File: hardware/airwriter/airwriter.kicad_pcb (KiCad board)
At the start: 2 copper layers, 62 x 104.3 mm, 130 parts, among them J1 USB-C 5V in, J2 Mini-DIN-8 to printer, J4 Mini-DIN-8 LocalTalk, SW1 EVQP44B3M side-press, SW3 TS-1002-BR16026, U1 ESP32-S3-WROOM-1-N8R2, U2 MAX3490ESA+, U3 MAX3232ESE+, U4 AP7361C-33E, U5 USBLC6-2SC6, U6 SP3485EN-L, U7 PIC12F1840-I/P, U8 SP3485EN-L, U9 74AHCT1G125SE-7

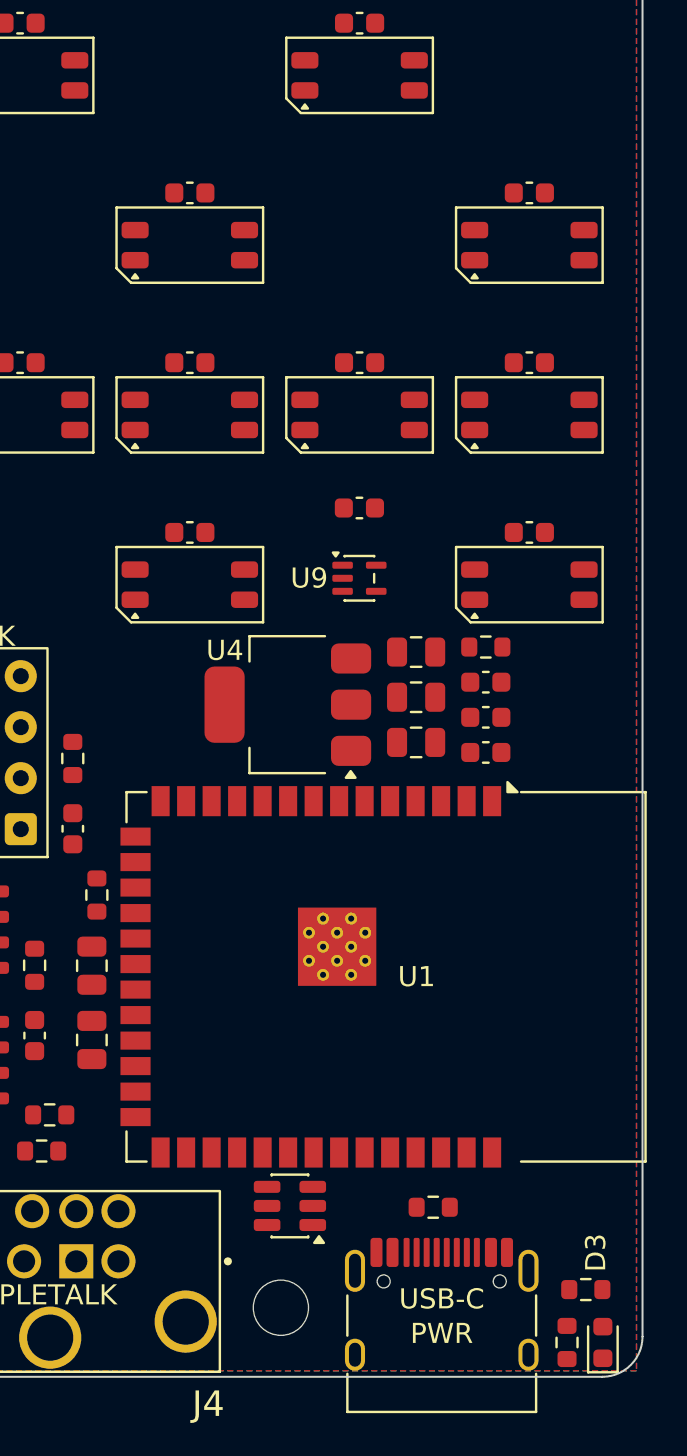
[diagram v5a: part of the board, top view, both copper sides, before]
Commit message: Lift the module for the corner mount
The two lower mounts sit level now, on the same columns as the upper pair:
H3 (105.636, 151.930) and H4 (156.364, 151.930). Four holes, one
rectangle, 50.7 x 86.3mm, support hull 505 -> 4378mm2.

H4's y is read off H3 rather than typed, so "level" is a property of the
placement instead of two numbers someone has to remember to edit together.
That makes J2 -- which caps H3 at y <= 152.034 -- set both, and it takes
J1 out of the picture: J1 alone would have allowed 154.214, and the level
pair sits north of that.

U1 lifts 4.556mm north to (149.250, 139.794), the minimum that clears
H4's courtyard by 0.2mm. Its south pad row gains 4.6mm to J4, so round
6's /HSKI_DRV pinch is far better than it was.

THE ANTENNA PAYS FOR THIS, on both edges, and the numbers are the point:

  north   the keepout's edge is clamped at the grid boundary y=127.6 so it
          stays out of the LED field, giving up 2.556mm of the lift. RF
          margin north of the radiator: 5.750 -> 3.194mm.
  south   notched around H4: on a 3.009mm-wide strip the clearance goes
          5.750 -> 0.495mm. Radiator south edge y=148.794; H4's drill edge
          is 1.761mm south of it, its courtyard 0.695mm, and a 5mm nut or
          boss would come within 0.636mm.

The lift closes the north-east strip to a band 2.094mm tall once a 1.0mm
escape channel is reserved above U1's north pad row -- reserved before
placing, not recovered after, because fourteen signals leave that row and
a distance-minimising solver packs caps straight onto it. That is how
round 6 lost /HSKI_DRV on the other side.

The band seats three parts, not five: dot (7,4)'s lit envelope blocks its
west end and (7,6)'s its east. So C9 (U1's rail 100n) takes 3.29mm from
pad 2, C2 (the 10u bulk) 6.32mm and C6 (the EN cap) 8.01mm, ordered by
what the module needs nearest rather than by package size. C5 is a
supplementary 100n redundant with C9 and R3 is a pull-up free on its own
nets, so those two travel 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
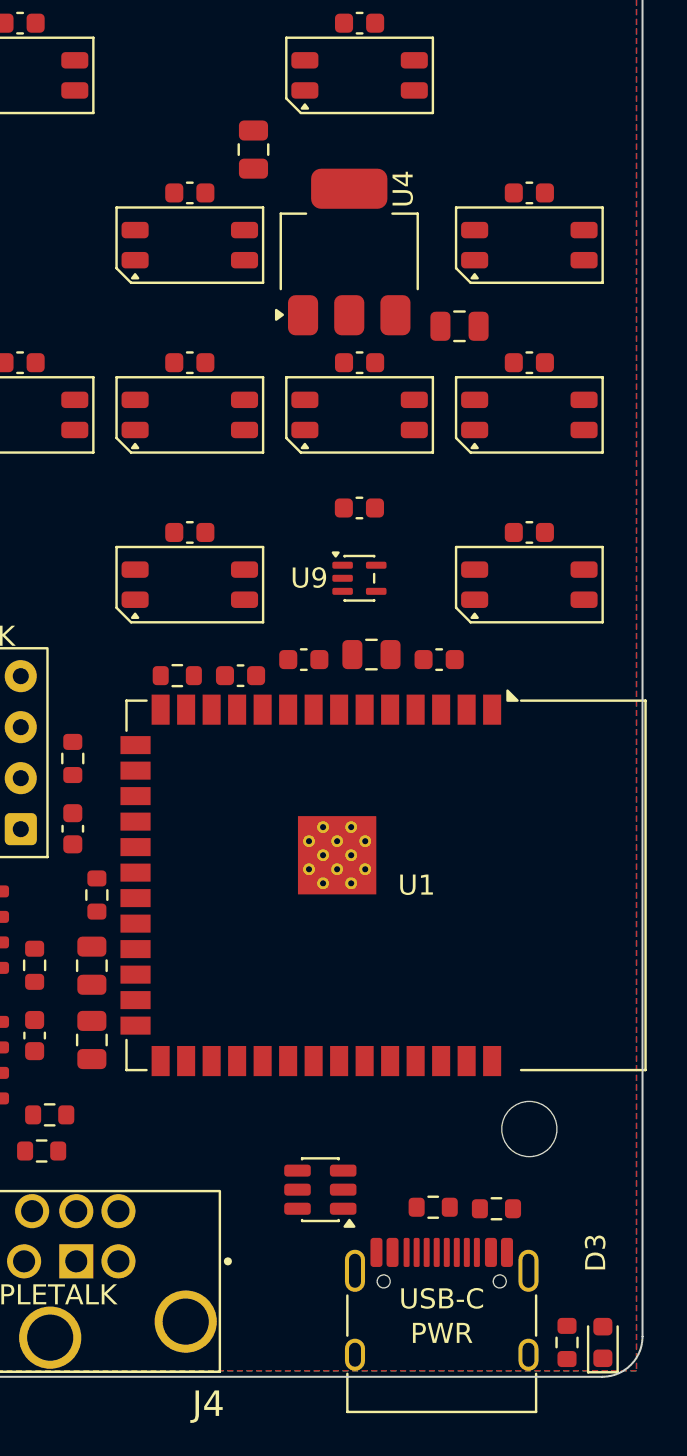
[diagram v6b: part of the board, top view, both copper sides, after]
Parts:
- moved C21 30.6 mm to (142.6, 103.2), turned to 90 degrees
- moved U4 22.8 mm to (147.4, 108.2), turned to 90 degrees
- moved C4 16.4 mm to (152.9, 112.0)
- moved R3 15.4 mm to (138.8, 129.3)
- moved H4 15.2 mm to (156.4, 151.9)
- moved C5 12.2 mm to (142.0, 129.3)
- moved C6 9.51 mm to (145.1, 128.6)
- moved R2 6.00 mm to (154.7, 155.9)
- moved C9 5.18 mm to (151.9, 128.6)
- moved U1 4.56 mm to (149.2, 139.8)
- moved C2 3.08 mm to (148.5, 128.3)
- moved U5 1.72 mm to (146.0, 154.9)
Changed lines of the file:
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@@
 	(footprint "Capacitor_SMD:C_0805_2012Metric"
 		(layer "F.Cu")
-		(at 150.725 130.425)
+		(at 148.5 128.3)
 		(descr "Capacitor SMD 0805 (2012 Metric), square (rectangular) end terminal, IPC-7351 nominal, (Body size source: IPC-SM-782 page 76, https://www.pcb-3d.com/wordpress/wp-content/uploads/ipc-sm-782a_amendment_1_and_2.pdf, https://docs.google.com/spreadsheets/d/1BsfQQcO9C6DZCsRaXUlFlo91Tg2WpOkGARC1WS5S8t0/edit?usp=sharing)")
 		(tags "capacitor")
@@
 	(footprint "Capacitor_SMD:C_0805_2012Metric"
 		(layer "F.Cu")
-		(at 150.725 128.175)
+		(at 152.884 111.95)
 		(descr "Capacitor SMD 0805 (2012 Metric), square (rectangular) end terminal, IPC-7351 nominal, (Body size source: IPC-SM-782 page 76, https://www.pcb-3d.com/wordpress/wp-content/uploads/ipc-sm-782a_amendment_1_and_2.pdf, https://docs.google.com/spreadsheets/d/1BsfQQcO9C6DZCsRaXUlFlo91Tg2WpOkGARC1WS5S8t0/edit?usp=sharing)")
 		(tags "capacitor")
@@
 	(footprint "Capacitor_SMD:C_0603_1608Metric"
 		(layer "F.Cu")
-		(at 154.195 133.175)
+		(at 151.87 128.55)
 		(descr "Capacitor SMD 0603 (1608 Metric), square (rectangular) end terminal, IPC-7351 nominal, (Body size source: IPC-SM-782 page 76, https://www.pcb-3d.com/wordpress/wp-content/uploads/ipc-sm-782a_amendment_1_and_2.pdf)")
 		(tags "capacitor")
@@
 	(footprint "Resistor_SMD:R_0603_1608Metric"
 		(layer "F.Cu")
-		(at 154.195 127.925)
+		(at 138.83 129.35)
 		(descr "Resistor SMD 0603 (1608 Metric), square (rectangular) end terminal, IPC-7351 nominal, (Body size source: IPC-SM-782 page 72, https://www.pcb-3d.com/wordpress/wp-content/uploads/ipc-sm-782a_amendment_1_and_2.pdf)")
 		(tags "resistor")
@@
 	(footprint "Package_TO_SOT_SMD:SOT-223-3_TabPin2"
 		(layer "F.Cu")
-		(at 144.335 130.795 180)
+		(at 147.394 108.25 90)
 		(descr "module CMS SOT223 4 pins")
 		(tags "CMS SOT")
 		(property "Reference" "U4"
-			(at 3.135 2.695 180)
+			(at 3.135 2.695 90)
 			(layer "F.SilkS")
 			(effects
@@
 		)
 		(property "Value" "AP7361C-33E"
-			(at 0 4.5 180)
+			(at 0 4.5 90)
 			(layer "F.Fab")
 			(effects
@@
 		)
 		(property "Datasheet" ""
-			(at 0 0 180)
+			(at 0 0 90)
 			(unlocked yes)
 			(layer "F.Fab")
@@
 		)
 		(property "Description" "LDO regulator, 3.3V fixed, 1A, SOT-223"
-			(at 0 0 180)
+			(at 0 0 90)
 			(unlocked yes)
 			(layer "F.Fab")
@@
 		)
 		(property "MPN" "AP7361C-33E-13"
-			(at 0 0 180)
+			(at 0 0 90)
 			(unlocked yes)
 			(layer "F.Fab")
@@
 		)
 		(property "Manufacturer" "Diodes Incorporated"
-			(at 0 0 180)
+			(at 0 0 90)
 			(unlocked yes)
 			(layer "F.Fab")
@@
 		(duplicate_pad_numbers_are_jumpers no)
 		(fp_line
-			(start 1.91 3.41)
-			(end 1.91 2.15)
+			(start 1.91 -3.41)
+			(end 1.91 -2.15)
 			(stroke
 				(width 0.12)
@@
 		)
 		(fp_line
-			(start 1.91 -3.41)
-			(end 1.91 -2.15)
+			(start -1.85 -3.41)
+			(end 1.91 -3.41)
 			(stroke
 				(width 0.12)
@@
 		)
 		(fp_line
-			(start -1.85 3.41)
-			(end 1.91 3.41)
+			(start 1.91 3.41)
+			(end 1.91 2.15)
 			(stroke
 				(width 0.12)
@@
 		)
 		(fp_line
-			(start -1.85 -3.41)
-			(end 1.91 -3.41)
+			(start -1.85 3.41)
+			(end 1.91 3.41)
 			(stroke
 				(width 0.12)
@@
 		)
 		(fp_line
-			(start 4.4 3.6)
-			(end 4.4 -3.6)
+			(start 4.4 -3.6)
+			(end -4.4 -3.6)
 			(stroke
 				(width 0.05)
@@
 		)
 		(fp_line
-			(start 4.4 -3.6)
-			(end -4.4 -3.6)
+			(start -4.4 -3.6)
+			(end -4.4 3.6)
 			(stroke
 				(width 0.05)
@@
 		)
 		(fp_line
-			(start -4.4 3.6)
-			(end 4.4 3.6)
+			(start 4.4 3.6)
+			(end 4.4 -3.6)
 			(stroke
 				(width 0.05)
@@
 		)
 		(fp_line
-			(start -4.4 -3.6)
-			(end -4.4 3.6)
+			(start -4.4 3.6)
+			(end 4.4 3.6)
 			(stroke
 				(width 0.05)
@@
 		)
 		(fp_line
-			(start -1.85 3.35)
-			(end 1.85 3.35)
+			(start -1.85 -2.35)
+			(end -0.85 -3.35)
 			(stroke
 				(width 0.1)
@@
 		(fp_line
 			(start -1.85 -2.35)
-			(end -0.85 -3.35)
+			(end -1.85 3.35)
 			(stroke
 				(width 0.1)
@@
 		)
 		(fp_line
-			(start -1.85 -2.35)
-			(end -1.85 3.35)
+			(start -1.85 3.35)
+			(end 1.85 3.35)
 			(stroke
 				(width 0.1)
@@
 		)
 		(fp_text user "${REFERENCE}"
-			(at 0 0 270)
+			(at 0 0 180)
 			(layer "F.Fab")
 			(effects
@@
 		)
 		(pad "1" smd roundrect
-			(at -3.15 -2.3 180)
+			(at -3.15 -2.3 90)
 			(size 2 1.5)
 			(layers "F.Cu" "F.Mask" "F.Paste")
@@
 		)
 		(pad "2" smd roundrect
-			(at -3.15 0 180)
+			(at -3.15 0 90)
 			(size 2 1.5)
 			(layers "F.Cu" "F.Mask" "F.Paste")
@@
 		)
 		(pad "2" smd roundrect
-			(at 3.15 0 180)
+			(at 3.15 0 90)
 			(size 2 3.8)
 			(layers "F.Cu" "F.Mask" "F.Paste")
@@
 		)
 		(pad "3" smd roundrect
-			(at -3.15 2.3 180)
+			(at -3.15 2.3 90)
 			(size 2 1.5)
 			(layers "F.Cu" "F.Mask" "F.Paste")
@@
 	(footprint "Capacitor_SMD:C_0805_2012Metric"
 		(layer "F.Cu")
-		(at 150.725 132.675)
+		(at 142.624 103.15 90)
 		(descr "Capacitor SMD 0805 (2012 Metric), square (rectangular) end terminal, IPC-7351 nominal, (Body size source: IPC-SM-782 page 76, https://www.pcb-3d.com/wordpress/wp-content/uploads/ipc-sm-782a_amendment_1_and_2.pdf, https://docs.google.com/spreadsheets/d/1BsfQQcO9C6DZCsRaXUlFlo91Tg2WpOkGARC1WS5S8t0/edit?usp=sharing)")
 		(tags "capacitor")
 		(property "Reference" "C21"
-			(at 0 -1.68 0)
+			(at 0 -1.68 90)
 			(layer "F.Fab")
 			(effects
@@
 		)
 		(property "Value" "22u"
-			(at 0 1.68 0)
+			(at 0 1.68 90)
 			(layer "F.Fab")
 			(effects
@@
 		)
 		(property "Datasheet" ""
-			(at 0 0 0)
+			(at 0 0 90)
 			(layer "F.Fab")
 			(hide yes)
@@
 		)
 		(property "Description" ""
-			(at 0 0 0)
+			(at 0 0 90)
 			(layer "F.Fab")
 			(hide yes)
@@
 		)
 		(property "KiLib_Generator" "SMD_2terminal_chip_molded"
-			(at 0 0 0)
+			(at 0 0 90)
 			(layer "F.SilkS")
 			(hide yes)
@@
 		)
 		(fp_text user "${REFERENCE}"
-			(at 0 0 0)
+			(at 0 0 90)
 			(layer "F.Fab")
 			(effects
@@
 		)
 		(pad "1" smd roundrect
-			(at -0.95 0)
+			(at -0.95 0 90)
 			(size 1 1.45)
 			(layers "F.Cu" "F.Mask" "F.Paste")
@@
 		)
 		(pad "2" smd roundrect
-			(at 0.95 0)
+			(at 0.95 0 90)
 			(size 1 1.45)
 			(layers "F.Cu" "F.Mask" "F.Paste")
@@
 	(footprint "Resistor_SMD:R_0603_1608Metric"
 		(layer "F.Cu")
-		(at 159.175 159.925)
+		(at 154.725 155.9)
 		(descr "Resistor SMD 0603 (1608 Metric), square (rectangular) end terminal, IPC-7351 nominal, (Body size source: IPC-SM-782 page 72, https://www.pcb-3d.com/wordpress/wp-content/uploads/ipc-sm-782a_amendment_1_and_2.pdf)")
 		(tags "resistor")
@@
 	(footprint "RF_Module:ESP32-S3-WROOM-1"
 		(layer "F.Cu")
-		(at 149.25 144.35 -90)
+		(at 149.25 139.794 -90)
 		(descr "2.4 GHz Wi-Fi and Bluetooth module  https://www.espressif.com/sites/default/files/documentation/esp32-s3-wroom-1_wroom-1u_datasheet_en.pdf")
 		(tags "2.4 GHz Wi-Fi and Bluetooth module")
@@
 			(polygon
 				(pts
-					(xy 156 129.6) (xy 162 129.6) (xy 162 159.1) (xy 157.6 159.1) (xy 157.6 156.6) (xy 156 156.6)
+					(xy 156 127.6) (xy 162 127.6) (xy 162 154.544) (xy 159.009 154.544) (xy 159.009 149.289) (xy 156 149.289)
 				)
 			)
@@
 	(footprint "Package_TO_SOT_SMD:SOT-23-6"
 		(layer "F.Cu")
-		(at 144.44 155.76 180)
+		(at 145.955 154.95 180)
 		(descr "SOT, 6 Pin (JEDEC MO-178 Var AB https://www.jedec.org/document_search?search_api_views_fulltext=MO-178)")
 		(tags "SOT TO_SOT_SMD")
@@
 	(footprint "Capacitor_SMD:C_0603_1608Metric"
 		(layer "F.Cu")
-		(at 154.195 129.675)
+		(at 141.98 129.35)
 		(descr "Capacitor SMD 0603 (1608 Metric), square (rectangular) end terminal, IPC-7351 nominal, (Body size source: IPC-SM-782 page 76, https://www.pcb-3d.com/wordpress/wp-content/uploads/ipc-sm-782a_amendment_1_and_2.pdf)")
 		(tags "capacitor")
@@
 	(footprint "Capacitor_SMD:C_0603_1608Metric"
 		(layer "F.Cu")
-		(at 154.195 131.425)
+		(at 145.13 128.55)
 		(descr "Capacitor SMD 0603 (1608 Metric), square (rectangular) end terminal, IPC-7351 nominal, (Body size source: IPC-SM-782 page 76, https://www.pcb-3d.com/wordpress/wp-content/uploads/ipc-sm-782a_amendment_1_and_2.pdf)")
 		(tags "capacitor")
@@
 	(footprint "MountingHole:MountingHole_2.2mm_M2"
 		(layer "F.Cu")
-		(at 143.99 160.83)
+		(at 156.364 151.93)
 		(descr "Mounting Hole 2.2mm, M2, no annular, generated by kicad-footprint-generator mountinghole.py")
 		(tags "mountinghole M2")

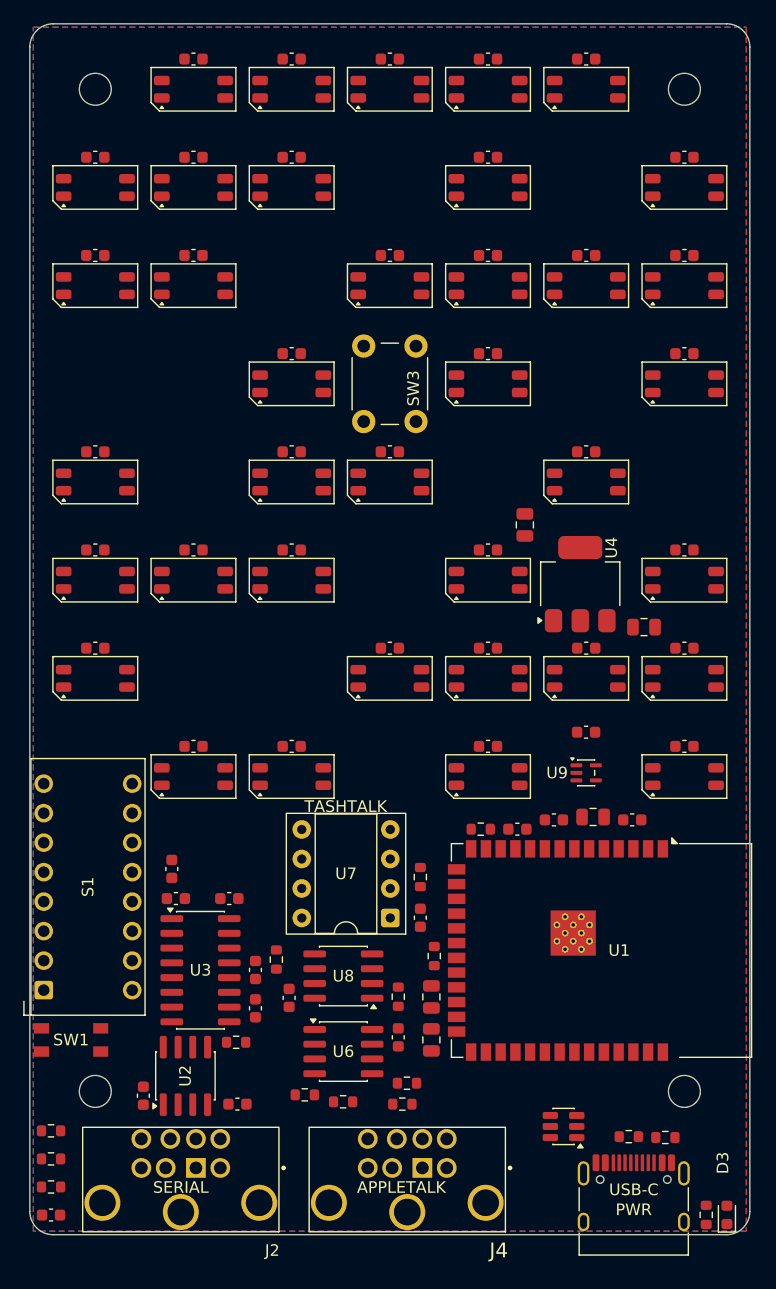
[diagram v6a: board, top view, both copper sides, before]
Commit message: Move H4 to the corner, restore the antenna keepout, route
H4 to (153.364, 151.93): 3mm west, clear of the WROOM radiator. Its
courtyard east edge (155.809) no longer enters the keepout (west 156.0),
so the keepout is restored from its H4 notch to a full rectangle
(156-162, 127.6-154.544). The antenna's south margin goes 0.495 -> 5.750mm.

Committed route: 838 segs / 66 routing vias + 23 stitching vias, score
993.43, 0 real breaks. DRC at the benign baseline (5 silk-edge, 5
lib_footprint_mismatch, 1 TASHTALK silk_overlap; 50 known parity issues).
Drills >=0.300mm, clearance >=0.15mm.

Route relief (disclosed): the H4-west shift squeezed J1's power-pad lane
and freerouting dropped a single marginal net. Widening its via-drop
pocket -- R15 +0.65mm and C16 +1.0mm north, both internal LocalTalk
passives -- reopened it. U1 unchanged.
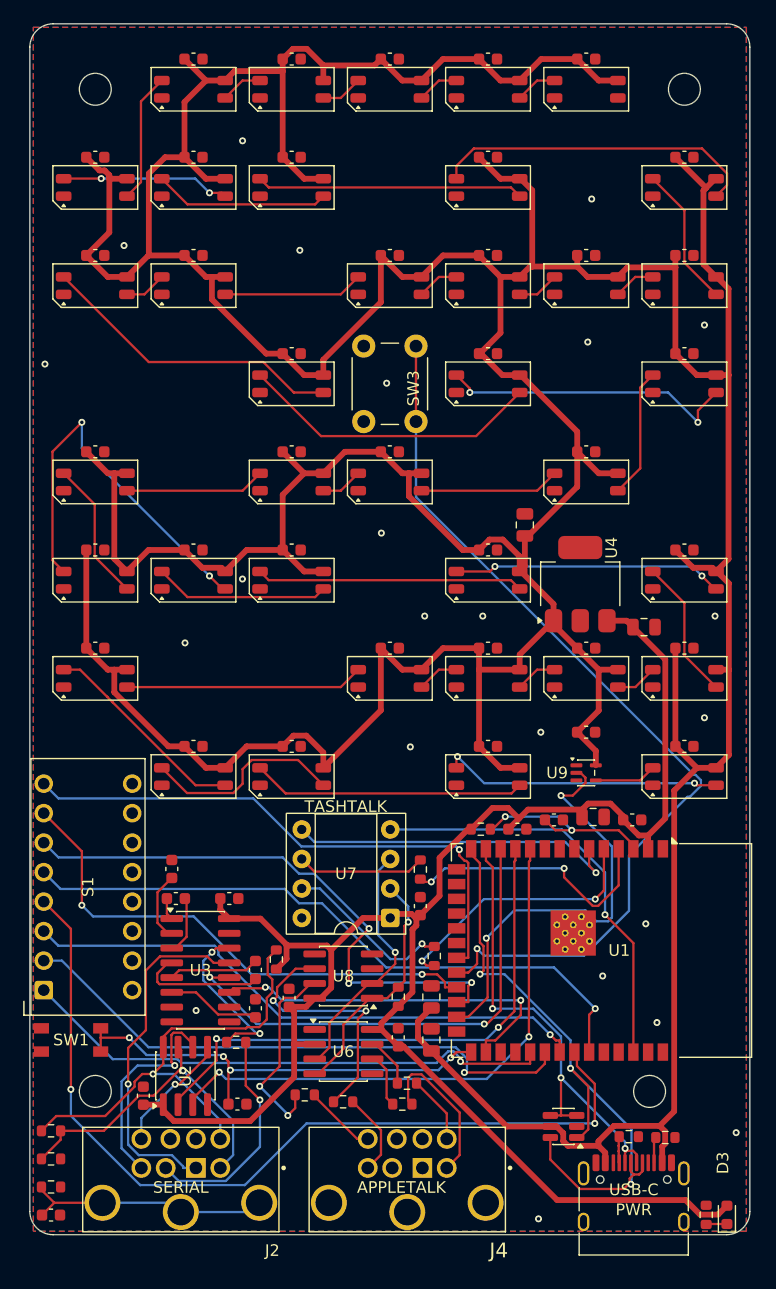
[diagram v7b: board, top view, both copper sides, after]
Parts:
- moved H4 3.00 mm to (153.4, 151.9)
- moved C16 1.00 mm to (133.6, 136.0)
- moved R15 0.65 mm to (133.6, 132.8)
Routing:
- net /VBUS: track 0.00 -> 542.7 mm
- net /+3V3: track 0.00 -> 155.7 mm
- net /BTN_TEST: track 0.00 -> 79.9 mm, vias 0 -> 1
- net /DIP4: track 0.00 -> 76.1 mm, vias 0 -> 2
- net /USB_DP: track 0.00 -> 57.0 mm, vias 0 -> 3
- net /DIP5: track 0.00 -> 56.3 mm, vias 0 -> 1
- net /DIP6: track 0.00 -> 49.9 mm, vias 0 -> 3
- net /DIP3: track 0.00 -> 49.6 mm, vias 0 -> 1
- net /DIP2: track 0.00 -> 49.5 mm, vias 0 -> 1
- net /DIP8: track 0.00 -> 48.9 mm, vias 0 -> 1
- net /UART_TX: track 0.00 -> 48.4 mm, vias 0 -> 2
- net /UART_RX: track 0.00 -> 47.8 mm, vias 0 -> 2
- net /DIP1: track 0.00 -> 46.5 mm, vias 0 -> 1
- net /DIP7: track 0.00 -> 44.7 mm, vias 0 -> 2
- net /UART_CTS: track 0.00 -> 42.8 mm, vias 0 -> 2
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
